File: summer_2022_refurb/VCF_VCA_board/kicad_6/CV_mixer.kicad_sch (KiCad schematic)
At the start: 48 parts, among them SW501 SW_SPDT_center_off, U7 TL072, U8 TL072, U9 TL072

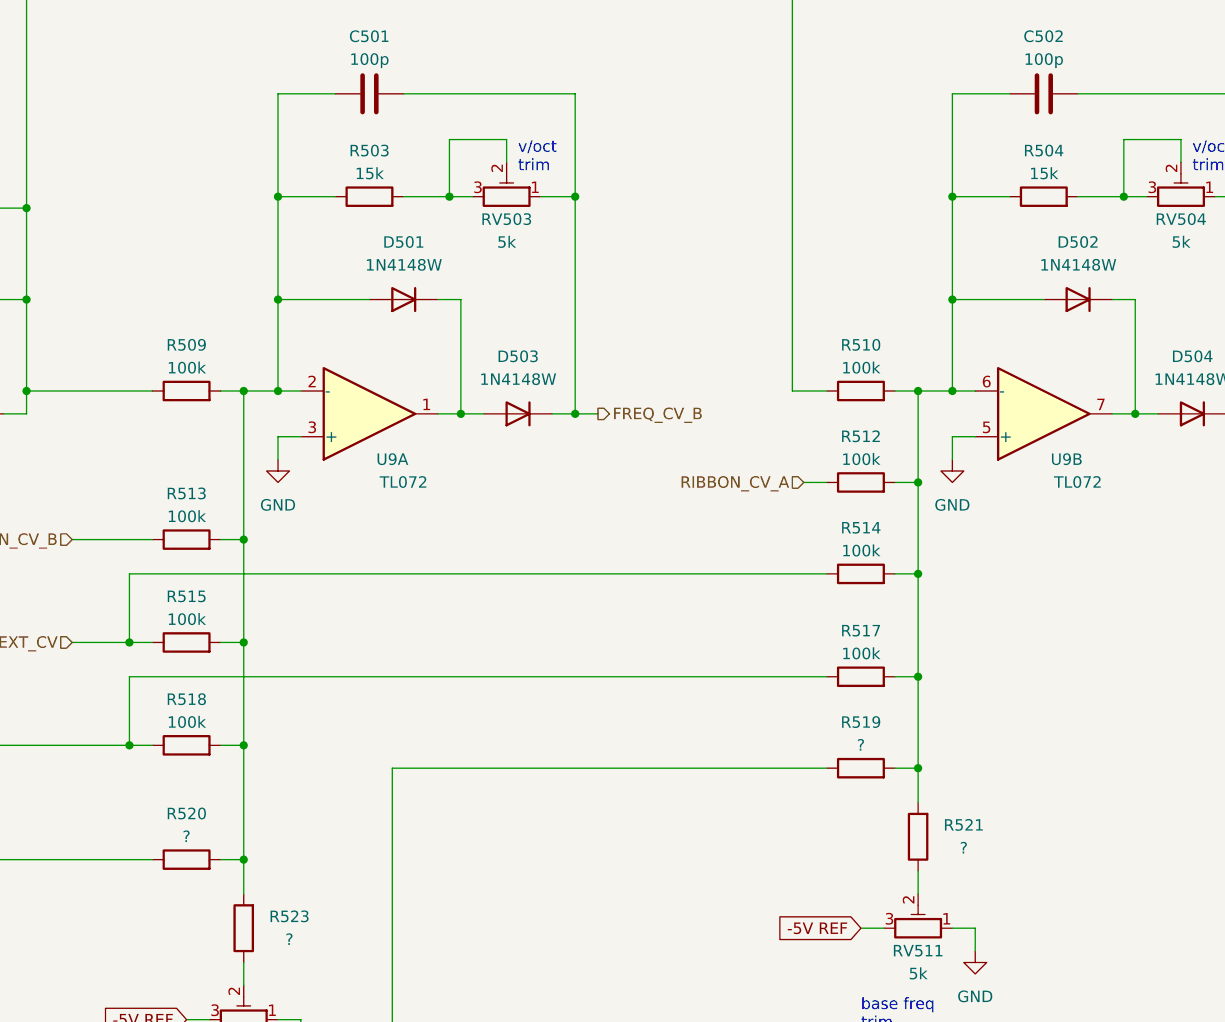
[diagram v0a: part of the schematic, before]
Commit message: Update VCF/VCA board
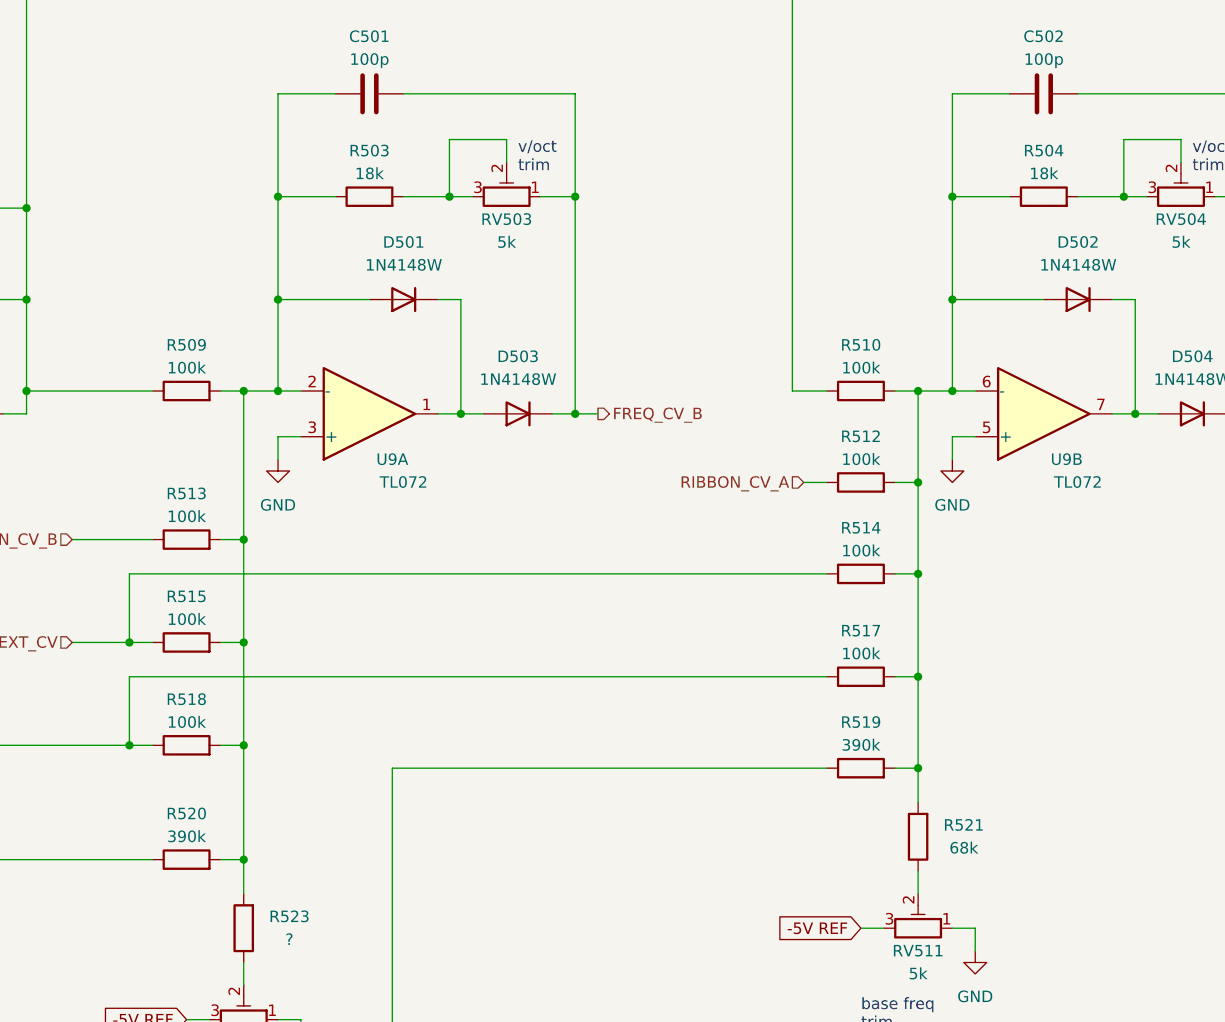
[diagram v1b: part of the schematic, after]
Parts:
- R503, R504: value 15k -> 18k
- R519, R520: value ? -> 390k
- R521: value ? -> 68k
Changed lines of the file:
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@@
     (in_bom yes) (on_board yes)
     (property "Reference" "R503" (id 0) (at 165.1 64.77 90))
-    (property "Value" "15k" (id 1) (at 165.1 67.31 90))
+    (property "Value" "18k" (id 1) (at 165.1 67.31 90))
     (property "Footprint" "Resistor_SMD:R_0805_2012Metric" (id 2) (at 165.1 71.628 90)
       (effects (font (size 1.27 1.27)) hide)
@@
     (in_bom yes) (on_board yes)
     (property "Reference" "R519" (id 0) (at 219.71 128.27 90))
-    (property "Value" "?" (id 1) (at 219.71 130.81 90))
+    (property "Value" "390k" (id 1) (at 219.71 130.81 90))
     (property "Footprint" "Resistor_SMD:R_0805_2012Metric" (id 2) (at 219.71 135.128 90)
       (effects (font (size 1.27 1.27)) hide)
@@
     (in_bom yes) (on_board yes)
     (property "Reference" "R521" (id 0) (at 231.14 139.7 0))
-    (property "Value" "?" (id 1) (at 231.14 142.24 0))
+    (property "Value" "68k" (id 1) (at 231.14 142.24 0))
     (property "Footprint" "Resistor_SMD:R_0805_2012Metric" (id 2) (at 227.838 140.97 90)
       (effects (font (size 1.27 1.27)) hide)
@@
     (in_bom yes) (on_board yes)
     (property "Reference" "R520" (id 0) (at 144.78 138.43 90))
-    (property "Value" "?" (id 1) (at 144.78 140.97 90))
+    (property "Value" "390k" (id 1) (at 144.78 140.97 90))
     (property "Footprint" "Resistor_SMD:R_0805_2012Metric" (id 2) (at 144.78 145.288 90)
       (effects (font (size 1.27 1.27)) hide)
@@
     (in_bom yes) (on_board yes)
     (property "Reference" "R504" (id 0) (at 240.03 64.77 90))
-    (property "Value" "15k" (id 1) (at 240.03 67.31 90))
+    (property "Value" "18k" (id 1) (at 240.03 67.31 90))
     (property "Footprint" "Resistor_SMD:R_0805_2012Metric" (id 2) (at 240.03 71.628 90)
       (effects (font (size 1.27 1.27)) hide)
